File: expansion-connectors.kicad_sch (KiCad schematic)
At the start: 3 parts

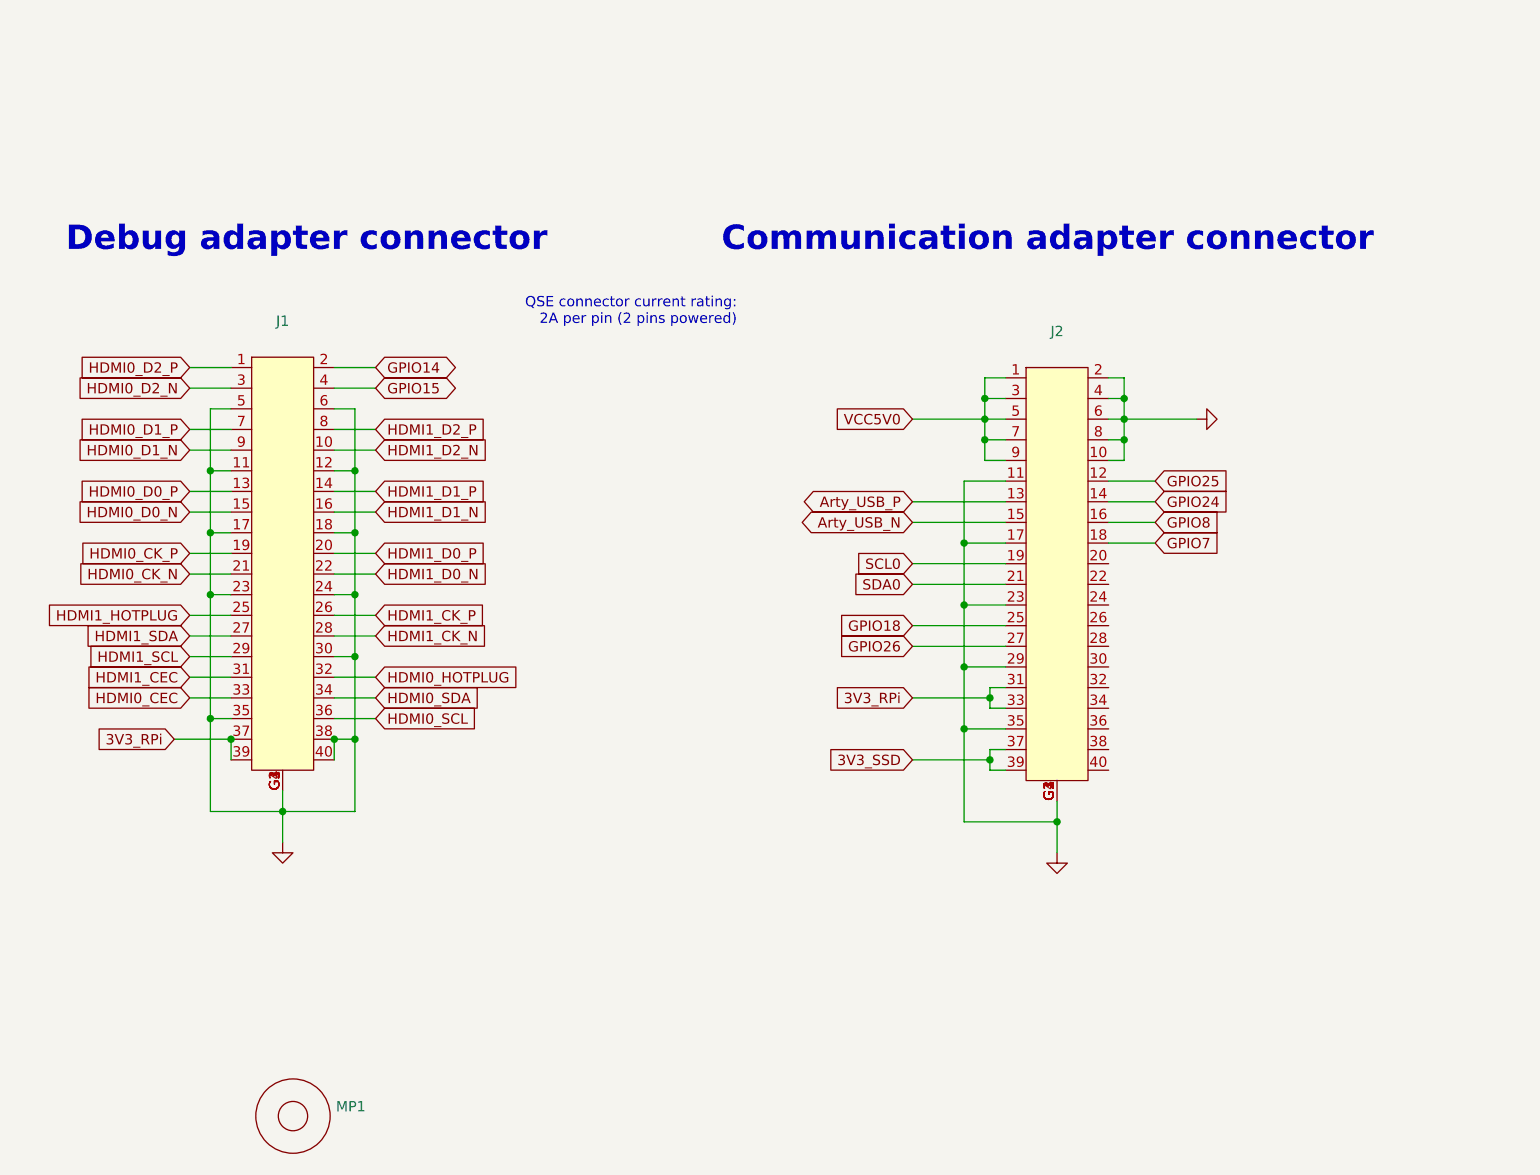
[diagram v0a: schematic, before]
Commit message: Exchanged flyback to CUI DCDC converter on schematics. Added logos.
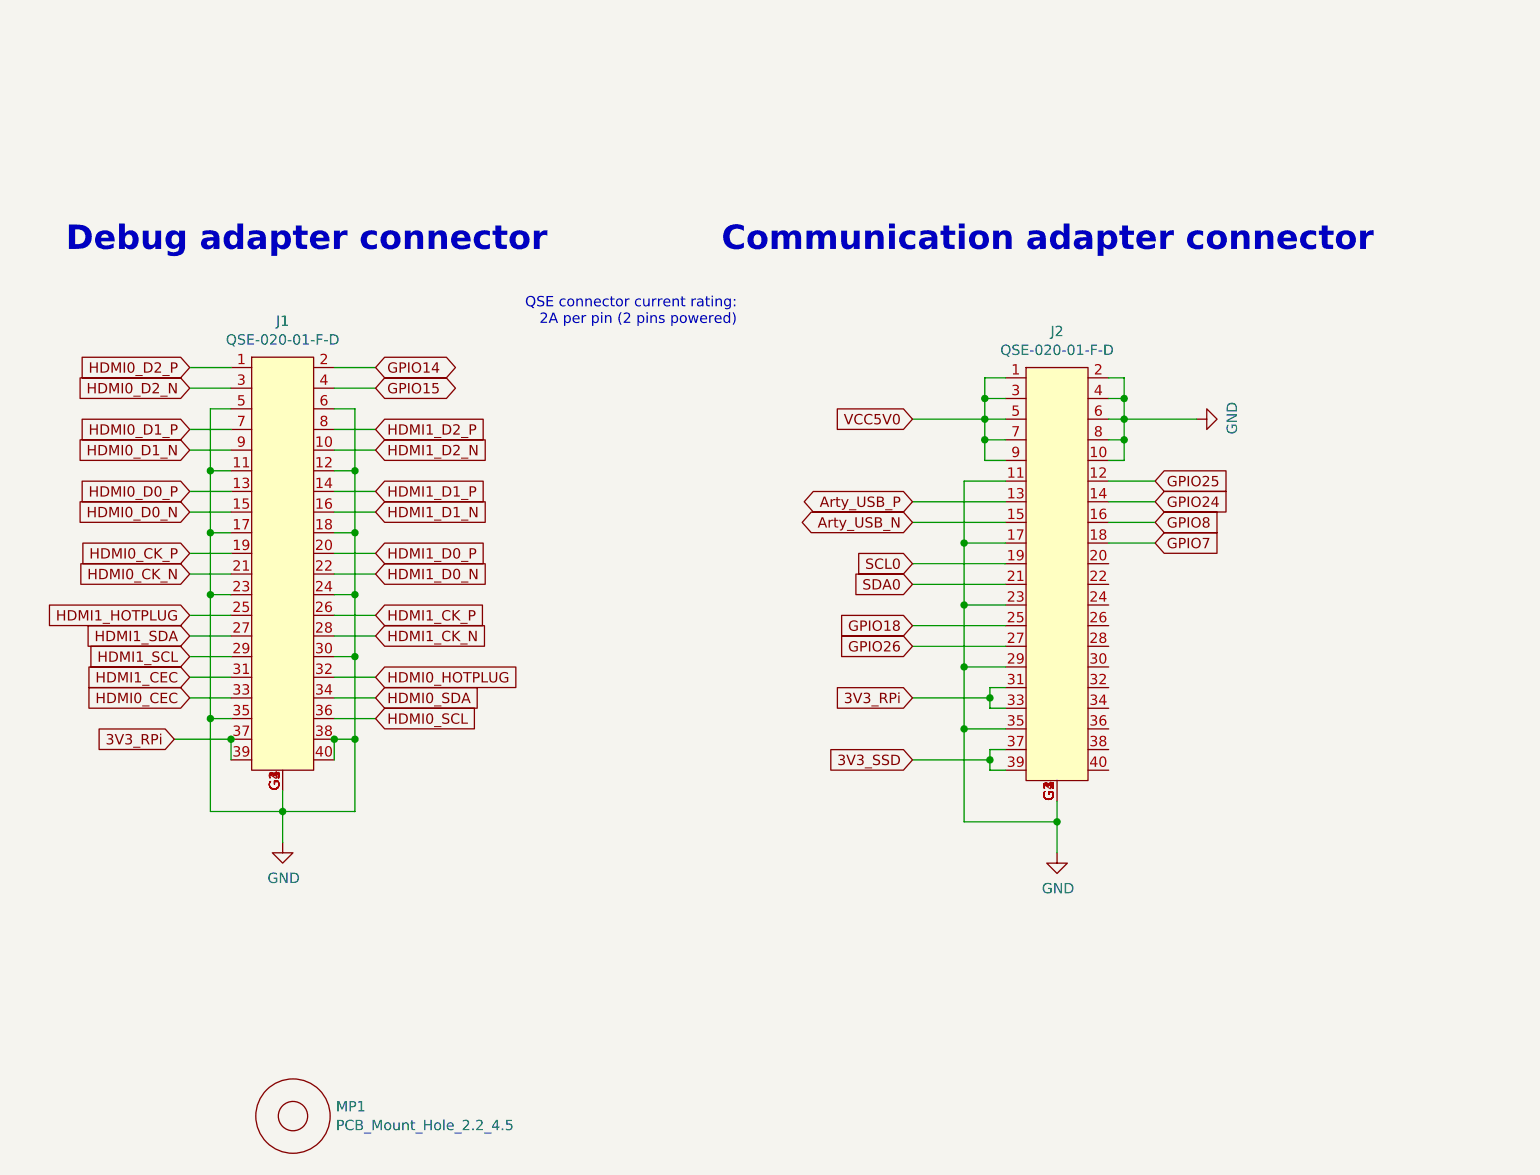
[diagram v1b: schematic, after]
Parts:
- J1, J2: value (none) -> QSE-020-01-F-D; footprint scalenode-footprints: -> scalenode-footprints:QSE-020-01-XXX-D-A
- MP1: value (none) -> PCB_Mount_Hole_2.2_4.5; footprint scalenode-footprints: -> scalenode-footprints:mounting-hole-2.2mm

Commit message: Added text fields with schematic descriptions
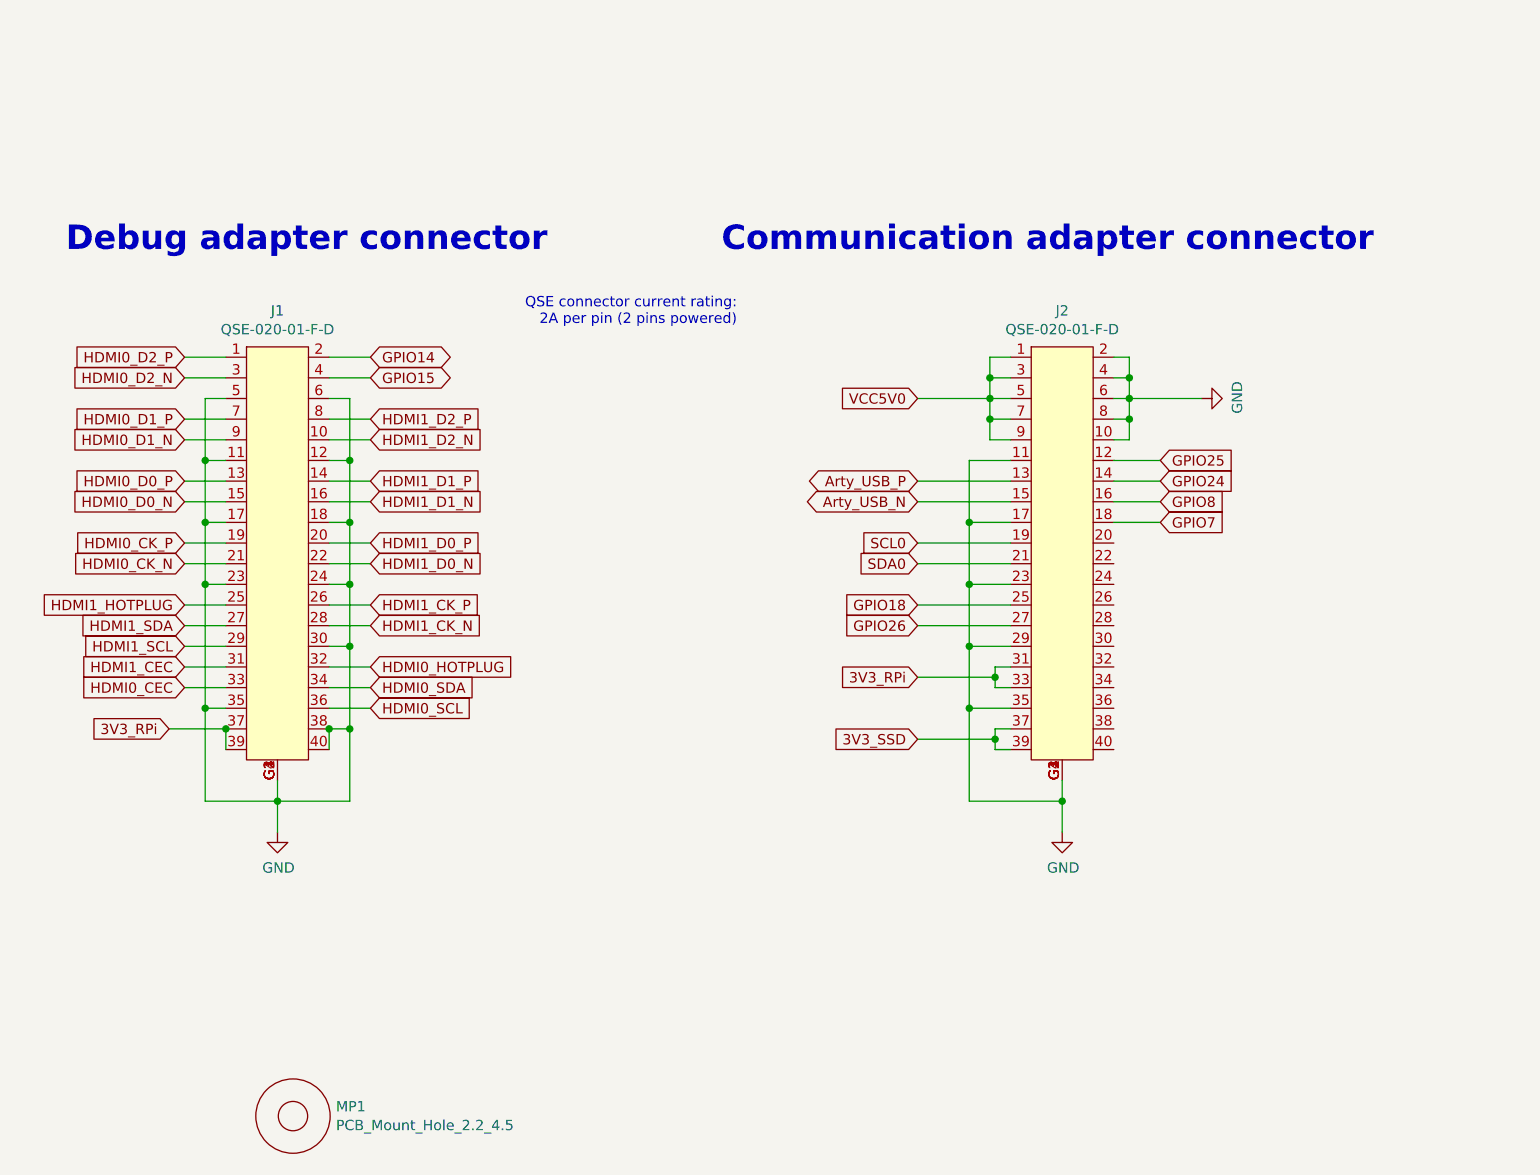
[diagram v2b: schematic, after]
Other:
- moved on the sheet: J1, J2

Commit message: Implemented changes from rev 1.0.4. New components initial placement
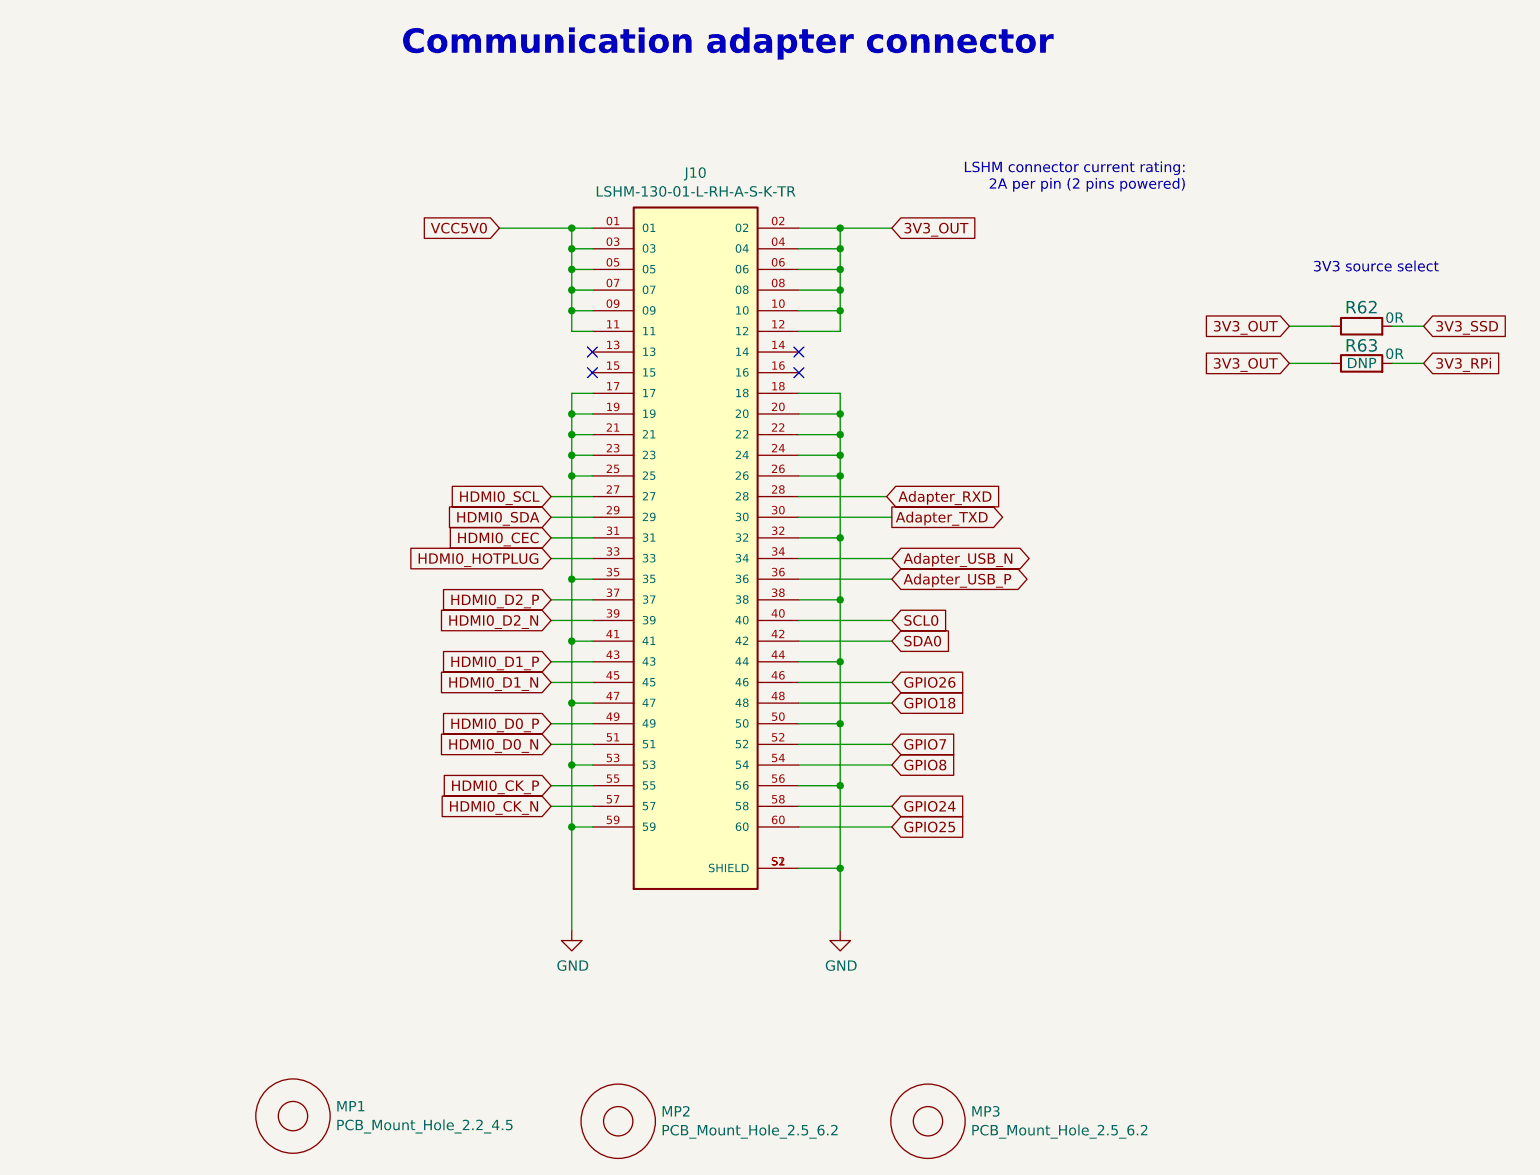
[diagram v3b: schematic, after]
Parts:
- removed J1, J2: QSE-020-01-F-D, scalenode-footprints:QSE-020-01-XXX-D-A, symbol scalenode:QSE-020-01-F-D
- added J10: LSHM-130-01-L-RH-A-S-K-TR, scalenode-footprints:SAMTEC_LSHM-130-01-XXX-RH-A-S-K-XX, symbol scalenode:LSHM-130-01-L-RH-A-S-K-TR
- added MP2, MP3: PCB_Mount_Hole_2.5_6.2, scalenode-footprints:Mount-hole-M2.5, symbol scalenode:PCB_Mount_Hole_2.5_6.2
- added R62, R63: R_0R_1206, scalenode-footprints:1206-res, symbol scalenode:R_0R_1206
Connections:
- net 3V3_RPi: now also R63.2
- net 3V3_SSD: now also R62.2
- net GND: now also J10.17, J10.18, J10.19, J10.20, J10.21, J10.22, J10.23, J10.24, J10.25, J10.26, J10.32, J10.35, J10.38, J10.41, J10.44, J10.47, J10.50, J10.53, J10.56, J10.59, J10.S1 (SHIELD), J10.S2 (SHIELD)
- net GPIO18: now also J10.48
- net GPIO24: now also J10.58
- net GPIO25: now also J10.60
- net GPIO26: now also J10.46
- net GPIO7: now also J10.52
- net GPIO8: now also J10.54
- net HDMI0_CEC: now also J10.31
- net HDMI0_CK_N: now also J10.57
- net HDMI0_CK_P: now also J10.55
- net HDMI0_D0_N: now also J10.51
- net HDMI0_D0_P: now also J10.49
- net HDMI0_D1_N: now also J10.45
- net HDMI0_D1_P: now also J10.43
- net HDMI0_D2_N: now also J10.39
- net HDMI0_D2_P: now also J10.37
- net HDMI0_HOTPLUG: now also J10.33
- net HDMI0_SCL: now also J10.27
- net HDMI0_SDA: now also J10.29
- net SCL0: now also J10.40
- net SDA0: now also J10.42
- net VCC5V0: now also J10.01, J10.03, J10.05, J10.07, J10.09, J10.11
- new net 3V3_OUT: J10.02, J10.04, J10.06, J10.08, J10.10, J10.12, R62.1, R63.1
- new net Adapter_RXD: J10.28
- new net Adapter_TXD: J10.30
- new net Adapter_USB_N: J10.34
- new net Adapter_USB_P: J10.36
- no-connect marks 0 -> 4
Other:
- note added: "3V3 source select"
- note added: "LSHM connector current rating: 2A per pin (2 pins powered)"
- note removed: "Debug adapter connector"
- note removed: "QSE connector current rating: 2A per pin (2 pins powered)"

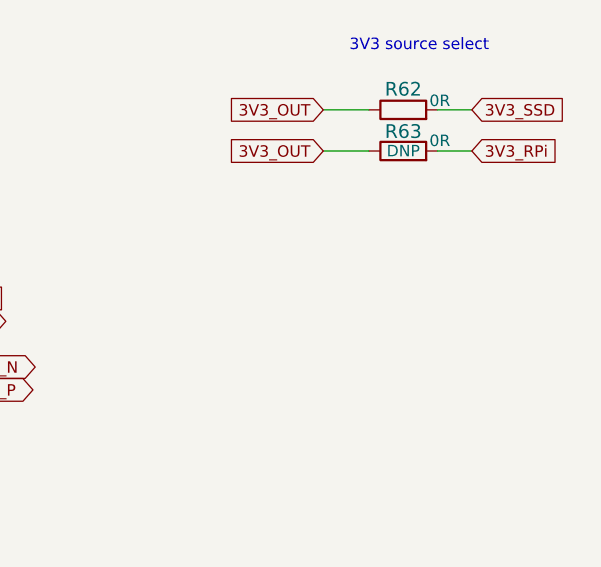
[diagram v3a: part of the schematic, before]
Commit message: Shortened board. Adjusted posiitons of components. Routed all signals. Added stitching cap
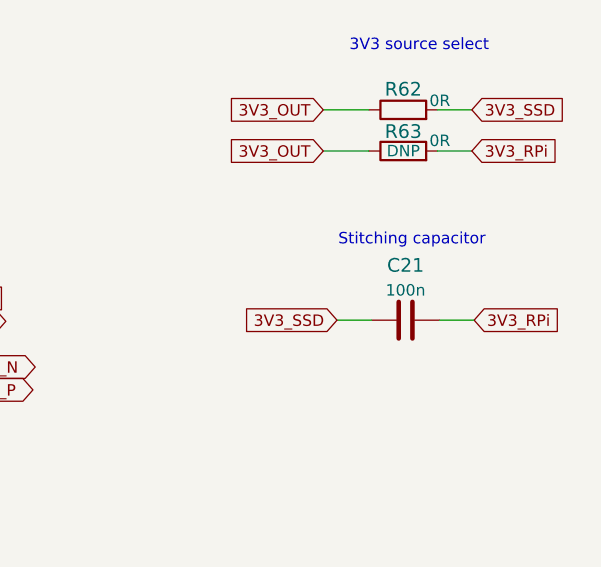
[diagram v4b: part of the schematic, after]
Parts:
- added C21: C_100n_0402, scalenode-footprints:0402-cap, symbol scalenode:C_100n_0402
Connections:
- net 3V3_RPi: now also C21.2
- net 3V3_SSD: now also C21.1
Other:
- note added: "Stitching capacitor"
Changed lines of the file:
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@@
+    (stroke (width 0) (type default) (color 0 0 0 0))
+  )
+  (wire (pts (xy 263.144 122.428) (xy 259.334 122.428))
     (stroke (width 0) (type default) (color 0 0 0 0))
   )
@@
   )
   (wire (pts (xy 172.085 127.635) (xy 167.005 127.635))
+    (stroke (width 0) (type default) (color 0 0 0 0))
+  )
+  (wire (pts (xy 270.764 122.428) (xy 274.574 122.428))
     (stroke (width 0) (type default) (color 0 0 0 0))
   )
@@
     (effects (font (size 1.27 1.27)) (justify right bottom))
   )
+  (text "Stitching capacitor" (at 275.844 114.3 180)
+    (effects (font (size 1.27 1.27)) (justify right bottom))
+  )
   (text "Communication adapter connector" (at 148.59 66.04 0)
     (effects (font (size 2.9972 2.9972) (thickness 0.5994) bold) (justify left bottom))
@@
     )
   )
+  (global_label "3V3_SSD" (shape input) (at 259.334 122.428 180) (fields_autoplaced)
+    (effects (font (size 1.27 1.27)) (justify right))
+    (property "Intersheet References" "${INTERSHEET_REFS}" (id 0) (at 534.289 220.853 0)
+      (effects (font (size 1.27 1.27)) hide)
+    )
+  )
   (global_label "HDMI0_SDA" (shape input) (at 167.005 122.555 180) (fields_autoplaced)
     (effects (font (size 1.27 1.27)) (justify right))
@@
     (effects (font (size 1.27 1.27)) (justify right))
     (property "Intersheet References" "${INTERSHEET_REFS}" (id 0) (at 0 0 0)
+      (effects (font (size 1.27 1.27)) hide)
+    )
+  )
+  (global_label "3V3_RPi" (shape input) (at 274.574 122.428 0) (fields_autoplaced)
+    (effects (font (size 1.27 1.27)) (justify left))
+    (property "Intersheet References" "${INTERSHEET_REFS}" (id 0) (at -2.921 19.558 0)
       (effects (font (size 1.27 1.27)) hide)
     )
@@
     (pin "1")
   )
+  (symbol (lib_id "scalenode:C_100n_0402") (at 266.954 122.428 90) (unit 1)
+    (in_bom yes) (on_board yes) (fields_autoplaced)
+    (property "Reference" "C21" (id 0) (at 266.954 116.3411 90)
+      (effects (font (size 1.524 1.524)))
+    )
+    (property "Value" "C_100n_0402" (id 1) (at 270.764 122.428 0)
+      (effects (font (size 1.524 1.524)) hide)
+    )
+    (property "Footprint" "scalenode-footprints:0402-cap" (id 2) (at 261.874 117.348 0)
+      (effects (font (size 1.524 1.524)) (justify left) hide)
+    )
+    (property "Datasheet" "" (id 3) (at 266.954 122.428 0)
+      (effects (font (size 1.27 1.27)) hide)
+    )
+    (property "Manufacturer" "Walsin" (id 4) (at 256.794 117.348 0)
+      (effects (font (size 1.524 1.524)) (justify left) hide)
+    )
+    (property "MPN" "0402X104K6R3CT" (id 5) (at 259.334 117.348 0)
+      (effects (font (size 1.524 1.524)) (justify left) hide)
+    )
+    (property "Val" "100n" (id 6) (at 266.954 119.1062 90))
+    (pin "1")
+    (pin "2")
+  )
 )
